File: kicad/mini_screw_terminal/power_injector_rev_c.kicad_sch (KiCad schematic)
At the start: 15 parts, among them J2 A00-108-220-450, J3 A00-108-220-450, J4 JACK-PLUG0

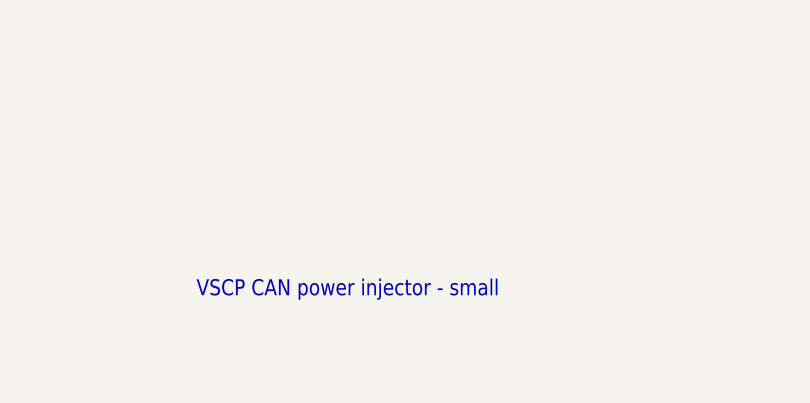
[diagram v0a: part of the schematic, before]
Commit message: Added screw terminal version
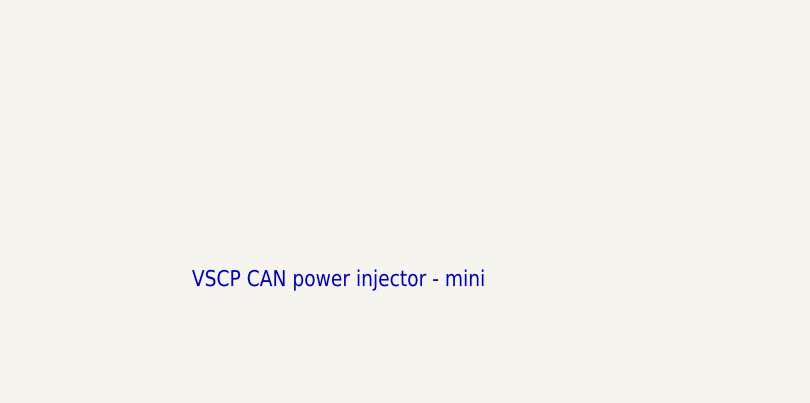
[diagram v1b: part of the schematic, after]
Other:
- note added: "VSCP CAN power injector - mini"
- note removed: "VSCP CAN power injector - small"
